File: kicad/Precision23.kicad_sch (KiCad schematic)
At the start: 21 parts, among them J501 Conn_01x02_Pin, J502 Conn_01x02_Pin, J503 Conn_02x03_Odd_Even, J504 Conn_01x06, J505 Conn_01x06, J506 Conn_01x05, J507 Conn_01x05, J508 Conn_01x06, J509 Conn_01x02_Pin, J596 STANDOFF, J597 STANDOFF, J598 STANDOFF, J599 STANDOFF, U501 SAM-M8Q, U502 NC7SZ157, U503 NC7SZ157, U504 NC7SZ157

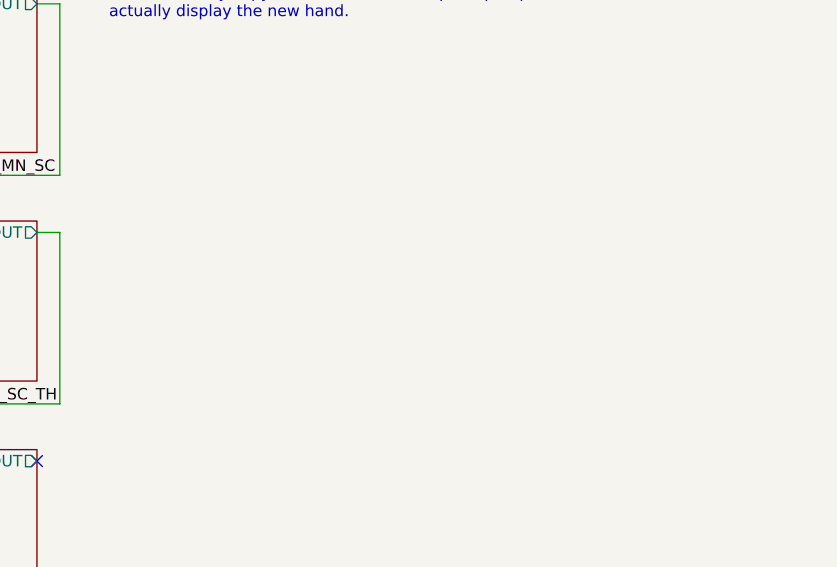
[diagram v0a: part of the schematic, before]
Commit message: Started on LPC21xx version
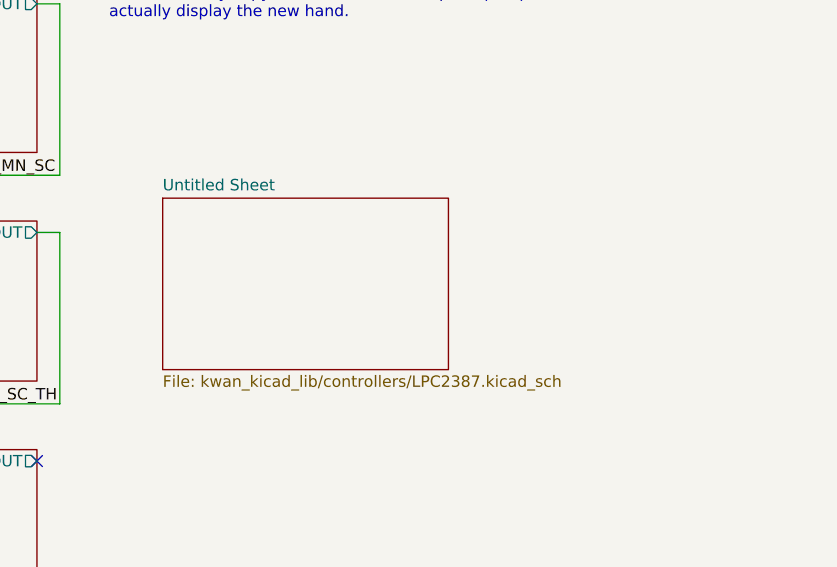
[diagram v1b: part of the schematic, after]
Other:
- added sheet Untitled Sheet (kwan_kicad_lib/controllers/LPC2387.kicad_sch)
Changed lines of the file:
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@@
+    )
+  )
+  (sheet (at 234.95 97.79) (size 31.75 19.05) (fields_autoplaced)
+    (stroke (width 0.1524) (type solid))
+    (fill (color 0 0 0 0.0000))
+    (property "Sheetname" "Untitled Sheet" (at 234.95 97.0784 0)
+      (effects (font (size 1.27 1.27)) (justify left bottom))
+    )
+    (property "Sheetfile" "kwan_kicad_lib/controllers/LPC2387.kicad_sch" (at 234.95 117.4246 0)
+      (effects (font (size 1.27 1.27)) (justify left top))
+    )
+    (instances
+      (project "Precision23"
+        (path "/9151f981-b383-4946-8df4-92ef46ef2206" (page "8"))
+      )
     )
   )
